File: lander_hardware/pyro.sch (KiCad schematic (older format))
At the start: 18 parts, among them J3 Pyro Channel, J4 Pyro Channel, J5 Pyro Channel, P6 CONN_02X03, P7 CONN_02X03, Q1 Q_NPN_CBE, Q2 Q_NPN_CBE, Q3 Q_NPN_CBE, U5 LM2902N

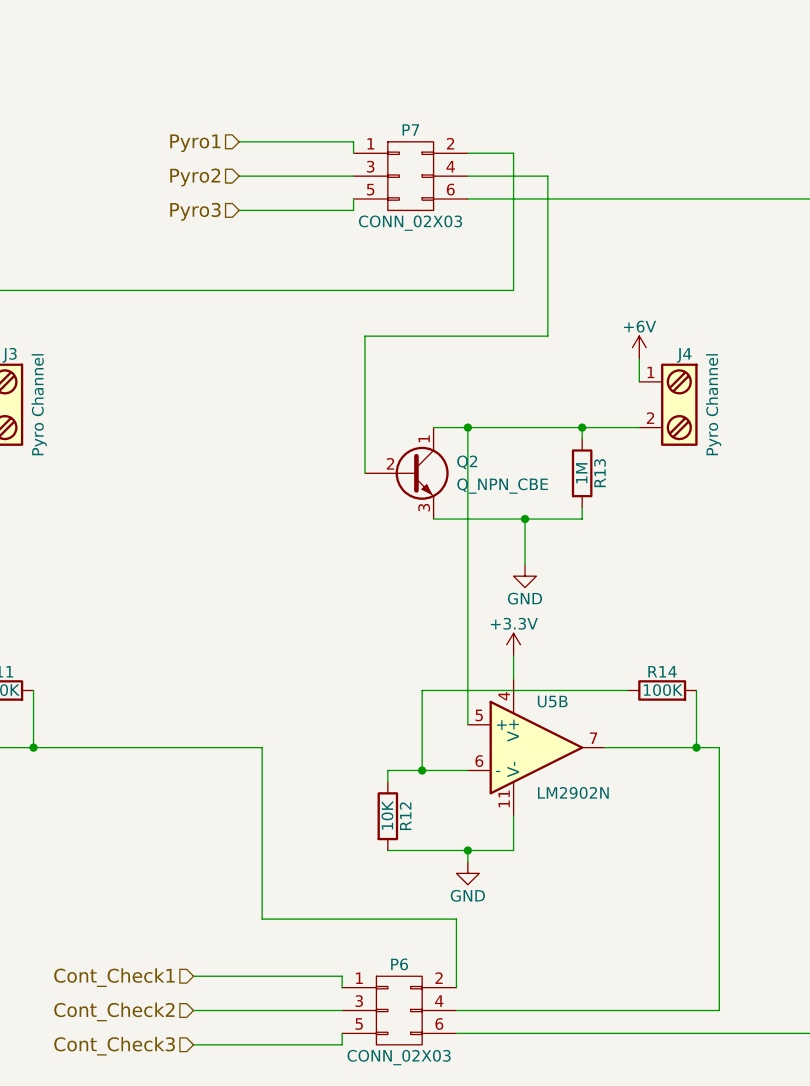
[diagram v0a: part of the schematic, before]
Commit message: Added ICSP
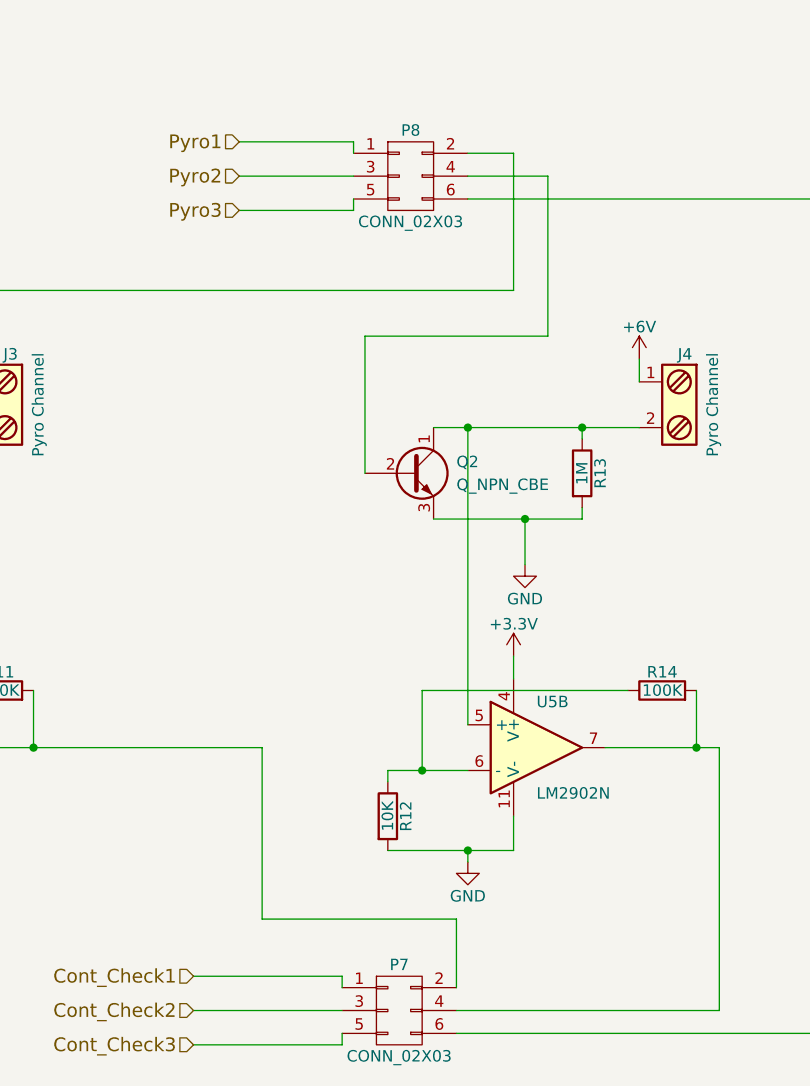
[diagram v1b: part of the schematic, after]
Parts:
- renumbered P6 to P7, P7 to P8
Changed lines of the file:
@@
 LIBS:dht11
 LIBS:BMP180
+LIBS:lander_1.0-cache
 EELAYER 25 0
 EELAYER END
@@
 $EndComp
 $Comp
-L GND #PWR030
+L GND #PWR35
 U 1 1 58A5FED3
 P 2300 2850
-F 0 "#PWR030" H 2300 2600 50  0001 C CNN
+F 0 "#PWR35" H 2300 2600 50  0001 C CNN
 F 1 "GND" H 2300 2700 50  0000 C CNN
 F 2 "" H 2300 2850 50  0000 C CNN
@@
 $EndComp
 $Comp
-L GND #PWR031
+L GND #PWR39
 U 1 1 58A5FEF9
 P 5200 2900
-F 0 "#PWR031" H 5200 2650 50  0001 C CNN
+F 0 "#PWR39" H 5200 2650 50  0001 C CNN
 F 1 "GND" H 5200 2750 50  0000 C CNN
 F 2 "" H 5200 2900 50  0000 C CNN
@@
 $EndComp
 $Comp
-L GND #PWR032
+L GND #PWR43
 U 1 1 58A5FFD3
 P 8050 2900
-F 0 "#PWR032" H 8050 2650 50  0001 C CNN
+F 0 "#PWR43" H 8050 2650 50  0001 C CNN
 F 1 "GND" H 8050 2750 50  0000 C CNN
 F 2 "" H 8050 2900 50  0000 C CNN
@@
 $EndComp
 $Comp
-L +6V #PWR033
+L +6V #PWR36
 U 1 1 58A6013C
 P 2750 2000
-F 0 "#PWR033" H 2750 1850 50  0001 C CNN
+F 0 "#PWR36" H 2750 1850 50  0001 C CNN
 F 1 "+6V" H 2750 2140 50  0000 C CNN
 F 2 "" H 2750 2000 50  0000 C CNN
@@
 $EndComp
 $Comp
-L +6V #PWR034
+L +6V #PWR40
 U 1 1 58A60162
 P 5700 2000
-F 0 "#PWR034" H 5700 1850 50  0001 C CNN
+F 0 "#PWR40" H 5700 1850 50  0001 C CNN
 F 1 "+6V" H 5700 2140 50  0000 C CNN
 F 2 "" H 5700 2000 50  0000 C CNN
@@
 $EndComp
 $Comp
-L +6V #PWR035
+L +6V #PWR44
 U 1 1 58A60188
 P 8550 2050
-F 0 "#PWR035" H 8550 1900 50  0001 C CNN
+F 0 "#PWR44" H 8550 1900 50  0001 C CNN
 F 1 "+6V" H 8550 2190 50  0000 C CNN
 F 2 "" H 8550 2050 50  0000 C CNN
@@
 $EndComp
 $Comp
-L +3.3V #PWR036
+L +3.3V #PWR34
 U 1 1 58A61402
 P 2250 3300
-F 0 "#PWR036" H 2250 3150 50  0001 C CNN
+F 0 "#PWR34" H 2250 3150 50  0001 C CNN
 F 1 "+3.3V" H 2250 3440 50  0000 C CNN
 F 2 "" H 2250 3300 50  0000 C CNN
@@
 $EndComp
 $Comp
-L +3.3V #PWR037
+L +3.3V #PWR38
 U 1 1 58A6142E
 P 5150 3300
-F 0 "#PWR037" H 5150 3150 50  0001 C CNN
+F 0 "#PWR38" H 5150 3150 50  0001 C CNN
 F 1 "+3.3V" H 5150 3440 50  0000 C CNN
 F 2 "" H 5150 3300 50  0000 C CNN
@@
 $EndComp
 $Comp
-L +3.3V #PWR038
+L +3.3V #PWR42
 U 1 1 58A6145A
 P 7950 3300
-F 0 "#PWR038" H 7950 3150 50  0001 C CNN
+F 0 "#PWR42" H 7950 3150 50  0001 C CNN
 F 1 "+3.3V" H 7950 3440 50  0000 C CNN
 F 2 "" H 7950 3300 50  0000 C CNN
@@
 $EndComp
 $Comp
-L CONN_02X03 P6
+L CONN_02X03 P7
 U 1 1 58A61592
 P 4650 4850
-F 0 "P6" H 4650 5050 50  0000 C CNN
+F 0 "P7" H 4650 5050 50  0000 C CNN
 F 1 "CONN_02X03" H 4650 4650 50  0000 C CNN
 F 2 "" H 4650 3650 50  0000 C CNN
@@
 $EndComp
 $Comp
-L GND #PWR039
+L GND #PWR33
 U 1 1 58A619FB
 P 2000 4150
-F 0 "#PWR039" H 2000 3900 50  0001 C CNN
+F 0 "#PWR33" H 2000 3900 50  0001 C CNN
 F 1 "GND" H 2000 4000 50  0000 C CNN
 F 2 "" H 2000 4150 50  0000 C CNN
@@
 $EndComp
 $Comp
-L GND #PWR040
+L GND #PWR37
 U 1 1 58A61A29
 P 4950 4200
-F 0 "#PWR040" H 4950 3950 50  0001 C CNN
+F 0 "#PWR37" H 4950 3950 50  0001 C CNN
 F 1 "GND" H 4950 4050 50  0000 C CNN
 F 2 "" H 4950 4200 50  0000 C CNN
@@
 $EndComp
 $Comp
-L GND #PWR041
+L GND #PWR41
 U 1 1 58A61ADD
 P 7700 4200
-F 0 "#PWR041" H 7700 3950 50  0001 C CNN
+F 0 "#PWR41" H 7700 3950 50  0001 C CNN
 F 1 "GND" H 7700 4050 50  0000 C CNN
 F 2 "" H 7700 4200 50  0000 C CNN
@@
 $EndComp
 $Comp
-L CONN_02X03 P7
+L CONN_02X03 P8
 U 1 1 58A6330E
 P 4700 1200
-F 0 "P7" H 4700 1400 50  0000 C CNN
+F 0 "P8" H 4700 1400 50  0000 C CNN
 F 1 "CONN_02X03" H 4700 1000 50  0000 C CNN
 F 2 "" H 4700 0   50  0000 C CNN
@@
 GNDin
 $Comp
-L +6V #PWR042
+L +6V #PWR32
 U 1 1 58B345BF
 P 1950 950
-F 0 "#PWR042" H 1950 800 50  0001 C CNN
+F 0 "#PWR32" H 1950 800 50  0001 C CNN
 F 1 "+6V" H 1950 1090 50  0000 C CNN
 F 2 "" H 1950 950 50  0000 C CNN
@@
 $EndComp
 $Comp
-L +3.3V #PWR043
+L +3.3V #PWR30
 U 1 1 58B345FB
 P 1800 700
-F 0 "#PWR043" H 1800 550 50  0001 C CNN
+F 0 "#PWR30" H 1800 550 50  0001 C CNN
 F 1 "+3.3V" H 1800 840 50  0000 C CNN
 F 2 "" H 1800 700 50  0000 C CNN
@@
 $EndComp
 $Comp
-L GND #PWR044
+L GND #PWR31
 U 1 1 58B34637
 P 1850 1200
-F 0 "#PWR044" H 1850 950 50  0001 C CNN
+F 0 "#PWR31" H 1850 950 50  0001 C CNN
 F 1 "GND" H 1850 1050 50  0000 C CNN
 F 2 "" H 1850 1200 50  0000 C CNN

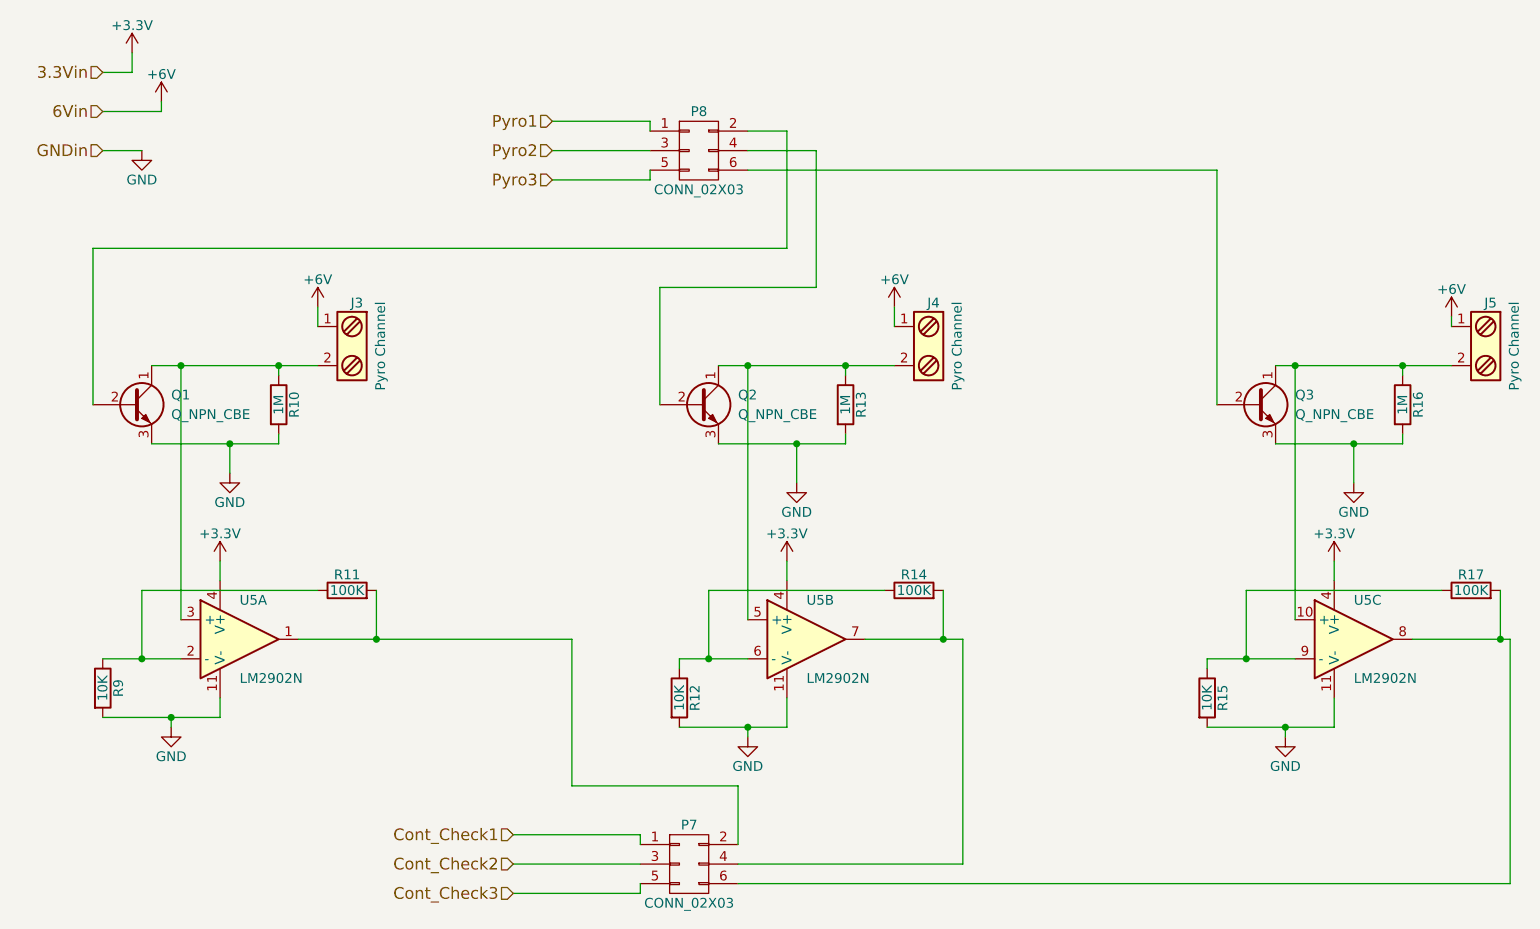
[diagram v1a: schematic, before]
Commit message: Simplified continuity tester
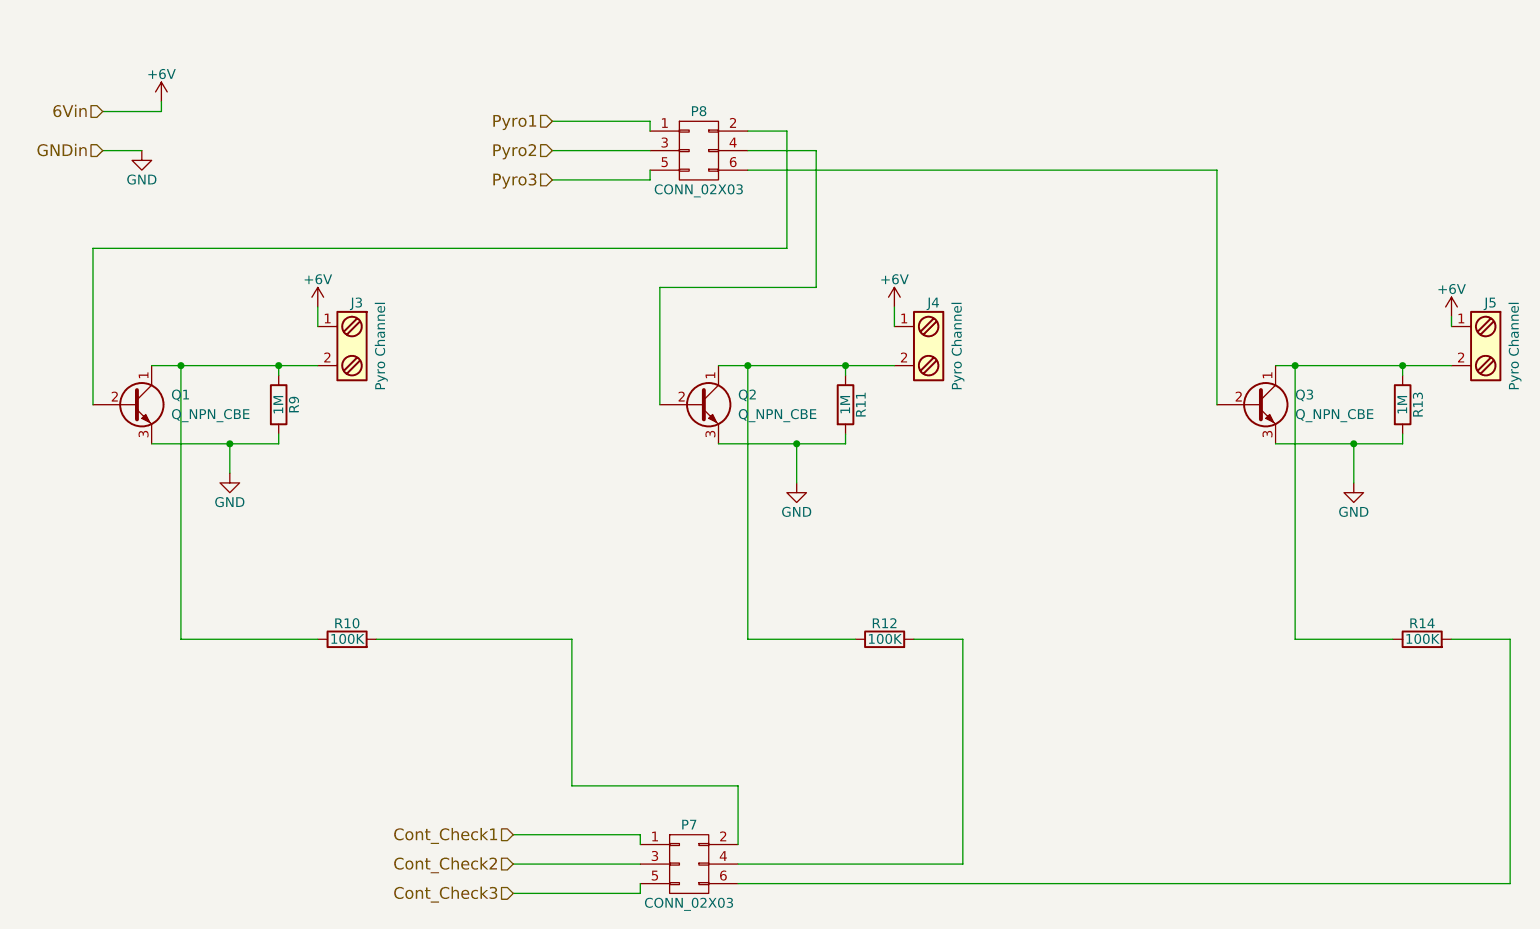
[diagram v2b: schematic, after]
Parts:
- removed R12, R15, R9: 10K, symbol R
- removed U5: LM2902N, symbol LM2902N
- renumbered R11 to R10, R13 to R11, R14 to R12, R16 to R13, R17 to R14, R10 to R9
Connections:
- net at J3.2, Q1.1 (C), R9.1: now also R10.1
- net at J4.2, Q2.1 (C), R11.1: now also R12.1
- net at J5.2, Q3.1 (C), R13.1: now also R14.1
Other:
- moved on the sheet: R10, R12, R14

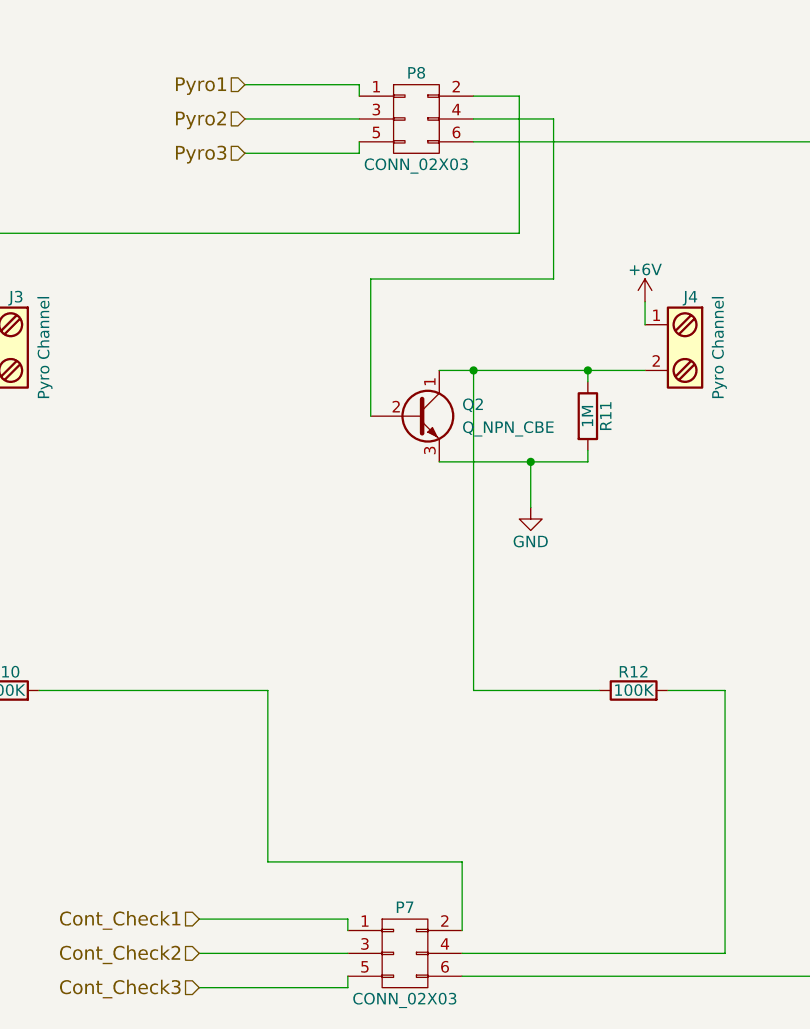
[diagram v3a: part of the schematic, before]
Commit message: Started associating footprints
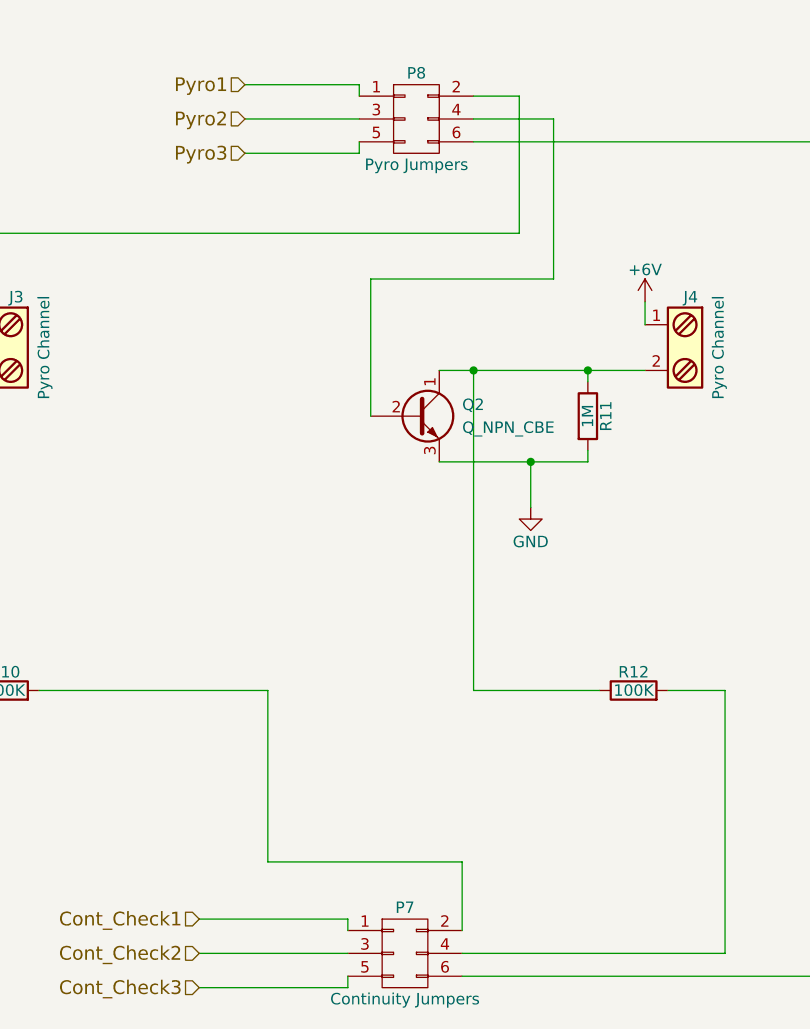
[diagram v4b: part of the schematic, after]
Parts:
- P7: value CONN_02X03 -> Continuity Jumpers
- P8: value CONN_02X03 -> Pyro Jumpers
- Q1, Q2, Q3: footprint (none) -> TO_SOT_Packages_THT:TO-220_Vertical
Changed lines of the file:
@@
 F 0 "Q1" H 2000 2550 50  0000 L CNN
 F 1 "Q_NPN_CBE" H 2000 2450 50  0000 L CNN
-F 2 "" H 2000 2600 50  0001 C CNN
+F 2 "TO_SOT_Packages_THT:TO-220_Vertical" H 2000 2600 50  0001 C CNN
 F 3 "" H 1800 2500 50  0000 C CNN
 	1    1800 2500
@@
 F 0 "Q2" H 4900 2550 50  0000 L CNN
 F 1 "Q_NPN_CBE" H 4900 2450 50  0000 L CNN
-F 2 "" H 4900 2600 50  0001 C CNN
+F 2 "TO_SOT_Packages_THT:TO-220_Vertical" H 4900 2600 50  0001 C CNN
 F 3 "" H 4700 2500 50  0000 C CNN
 	1    4700 2500
@@
 F 0 "Q3" H 7750 2550 50  0000 L CNN
 F 1 "Q_NPN_CBE" H 7750 2450 50  0000 L CNN
-F 2 "" H 7750 2600 50  0001 C CNN
+F 2 "TO_SOT_Packages_THT:TO-220_Vertical" H 7750 2600 50  0001 C CNN
 F 3 "" H 7550 2500 50  0000 C CNN
 	1    7550 2500
@@
 P 4650 4850
 F 0 "P7" H 4650 5050 50  0000 C CNN
-F 1 "CONN_02X03" H 4650 4650 50  0000 C CNN
+F 1 "Continuity Jumpers" H 4650 4650 50  0000 C CNN
 F 2 "" H 4650 3650 50  0001 C CNN
 F 3 "" H 4650 3650 50  0000 C CNN
@@
 P 4700 1200
 F 0 "P8" H 4700 1400 50  0000 C CNN
-F 1 "CONN_02X03" H 4700 1000 50  0000 C CNN
+F 1 "Pyro Jumpers" H 4700 1000 50  0000 C CNN
 F 2 "" H 4700 0   50  0001 C CNN
 F 3 "" H 4700 0   50  0000 C CNN
